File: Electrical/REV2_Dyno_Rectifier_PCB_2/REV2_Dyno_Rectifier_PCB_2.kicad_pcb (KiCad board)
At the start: 2 copper layers, 25 x 20 mm, 33 parts, among them J1 Dynamo Input, J2 Barrel_Jack_MountingPin, U1 TPS63070RNMR, U2 PAM2803AAF095

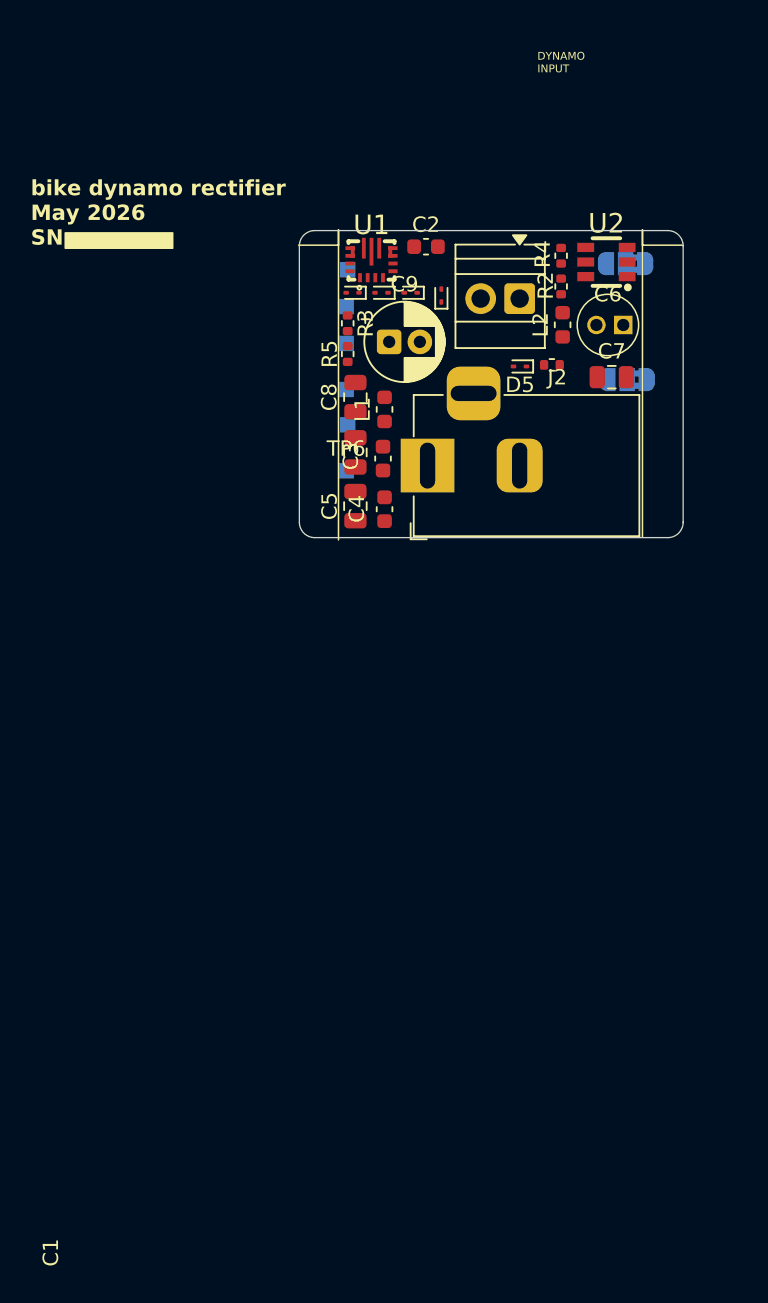
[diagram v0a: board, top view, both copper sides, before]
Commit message: schematic should be done! component placement almost done
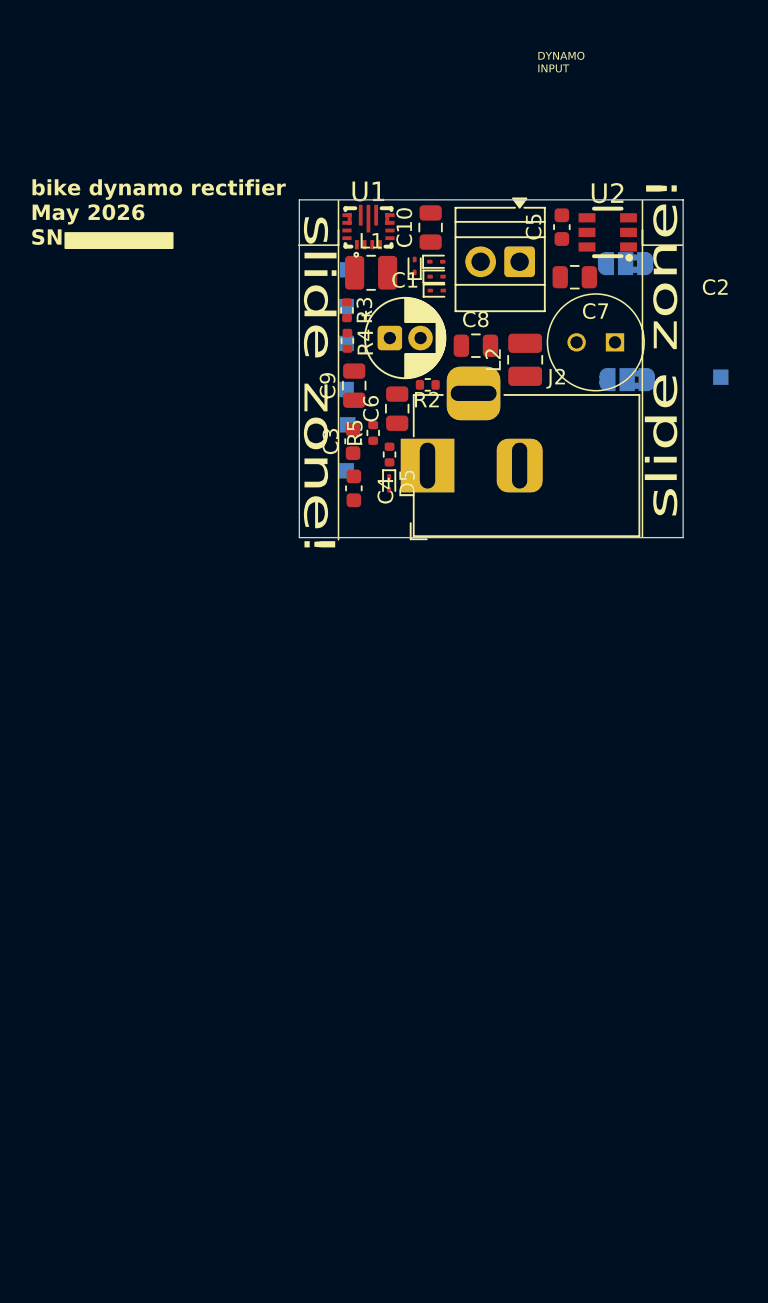
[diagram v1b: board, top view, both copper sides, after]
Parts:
- added C10: 10uF, Capacitor_SMD:C_0805_2012Metric, F.Cu at (62.8, 36.0)
- added TP6: TestPoint, TestPoint:TestPoint_Pad_1.0x1.0mm, B.Cu at (81.7, 45.8)
- L1, L2: footprint Inductor_SMD:L_0603_1608Metric -> Inductor_SMD:L_1008_2520Metric
- moved C5 21.7 mm to (71.3, 36.0)
- moved C2 18.3 mm to (72.2, 39.3), turned to 180 degrees
- moved R4 15.0 mm to (57.4, 43.4), turned to -90 degrees
- moved C3 13.5 mm to (57.8, 50.0), turned to 90 degrees
- moved R1 12.1 mm to (60.1, 50.8), turned to 90 degrees
- moved D5 11.4 mm to (60.1, 52.7), turned to -90 degrees
- moved R2 10.8 mm to (62.6, 46.3), turned to 180 degrees
- moved C8 9.08 mm to (65.8, 43.8)
- moved L1 8.94 mm to (58.9, 39.0), turned to 0 degrees
- moved C6 6.91 mm to (60.6, 47.9)
- moved D3 5.81 mm to (63.2, 38.3), turned to 0 degrees
- moved R5 5.40 mm to (59.1, 49.4)
- moved D2 3.61 mm to (63.2, 40.2), turned to 0 degrees
- moved L2 3.34 mm to (69.0, 44.7)
- moved C4 2.72 mm to (57.8, 53.0), turned to -90 degrees
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- renumbered C9 to C1, C1 to C2, C2 to C3, C3 to C4, C4 to C5, C5 to C6, C6 to C7, C7 to C8, C8 to C9, TP6 to TP7
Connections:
- D1 pad 1: Raw_Input -> Raw_Input_+
- D2 pad 1: GND -> Raw_Input_-
- D2 pad 2: Net-(D2-A) -> GND
- D3 pad 2: Raw_Input -> Raw_Input_+
- D4 pad 1: Net-(D2-A) -> Rectified
- D4 pad 2: Rectified -> Raw_Input_-
- J1 pad 1: Net-(D2-A) -> Raw_Input_-
- J1 pad 2: Raw_Input -> Raw_Input_+
- TP1 pad 1: 2.7V -> Raw_Input_+
- TP2 pad 1: Rectified -> Raw_Input_-
- TP3 pad 1: Raw_Input -> Rectified
- TP4 pad 1: V_out -> 2.7V
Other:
- board size 25 x 20 mm -> 25 x 22 mm
- board text added: "slide zone!"

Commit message: sent off rectifier PCB and the Light PCB off to JLCPCB tonight
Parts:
- added REF**: oshw mark, william_custom:oshw mark, F.Cu at (79.5, 37.6)
- added REF**: oshw mark, william_custom:oshw mark, F.Cu at (53.6, 52.9)
- added REF**: oshw mark, william_custom:oshw mark, B.Cu at (73.4, 54.0)
- R5: value 2.7 -> 1.8
- moved TP6 24.1 mm to (58.2, 51.3)
- moved JP2 3.13 mm to (73.9, 48.6)
- moved TP7 2.80 mm to (58.2, 54.5)
- moved JP1 1.85 mm to (73.7, 38.3)
- moved TP4 0.87 mm to (58.2, 46.6)
- moved TP3 0.79 mm to (58.1, 43.7)
- moved TP1 0.69 mm to (58.1, 38.9)
- moved TP5 0.69 mm to (58.1, 49.0)
- moved TP2 0.69 mm to (58.0, 41.3)
- moved C2 0.14 mm to (72.3, 39.3)
- moved R2 0.11 mm to (62.6, 46.4)
- moved J2 0.08 mm to (62.6, 51.6)
- moved C9 0.05 mm to (57.8, 46.4)
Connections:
- J2 pad 1: Out_Sleeve -> Out_Tip
- J2 pad 2: Out_Tip -> Out_Sleeve
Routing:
- net 2.7V: track 0.00 -> 62.5 mm, vias 0 -> 3
- net GND: track 0.00 -> 54.8 mm, vias 0 -> 13
- net Rectified: track 0.00 -> 52.7 mm, vias 0 -> 6
- net V_out: track 0.00 -> 49.5 mm, vias 0 -> 3
- net FB: track 0.00 -> 47.1 mm, vias 0 -> 2
- net Net-(D5-A): track 0.00 -> 43.9 mm
- net Out_Tip: track 0.00 -> 34.7 mm
- net Net-(R2-Pad2): track 0.00 -> 34.1 mm, vias 0 -> 4
- net Net-(U1-EN): track 0.00 -> 31.5 mm, vias 0 -> 2
- net Net-(U1-Vaux): track 0.00 -> 21.3 mm, vias 0 -> 2
- net Raw_Input_-: track 0.00 -> 15.9 mm, vias 0 -> 1
- net Raw_Input_+: track 0.00 -> 14.5 mm, vias 0 -> 2
- net Net-(U1-L1): track 0.00 -> 12.1 mm, vias 0 -> 2
- net Net-(U1-L2): track 0.00 -> 9.98 mm, vias 0 -> 2
- net Net-(U1-PG): track 0.00 -> 9.77 mm, vias 0 -> 4
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- added copper zone on B.Cu, net GND
- added copper zone on F.Cu, net GND
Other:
- outline, holes or cut-outs redrawn
- board text added: "2.7V"
- board text added: "FB"
- board text added: "GND"
- board text added: "Rev. 2 - May 2026"
- board text added: "US002271"
- board text added: "contactless bike dynamo rectifier"
- board text added: "dynamo input"
- board text added: "freakylamps w. kennedy SN:"
- board text added: "out"
- board text added: "raw in +"
- board text added: "raw in -"
- board text added: "rectified"
- board text added: "regulated"
- board text removed: "bike dynamo rectifier May 2026 SN:"
